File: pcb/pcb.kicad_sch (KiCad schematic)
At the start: 3 parts, among them U2 ESP32-C6-MINI-1

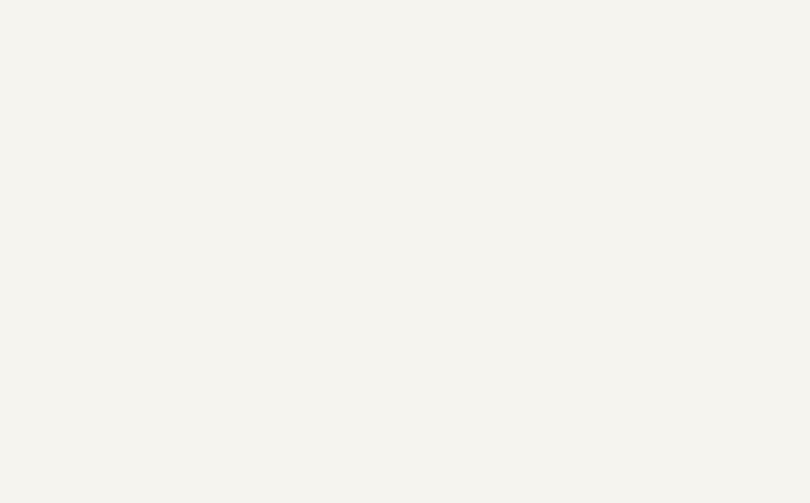
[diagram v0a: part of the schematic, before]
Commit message: adding the lightresistor with the voltage devider circuit
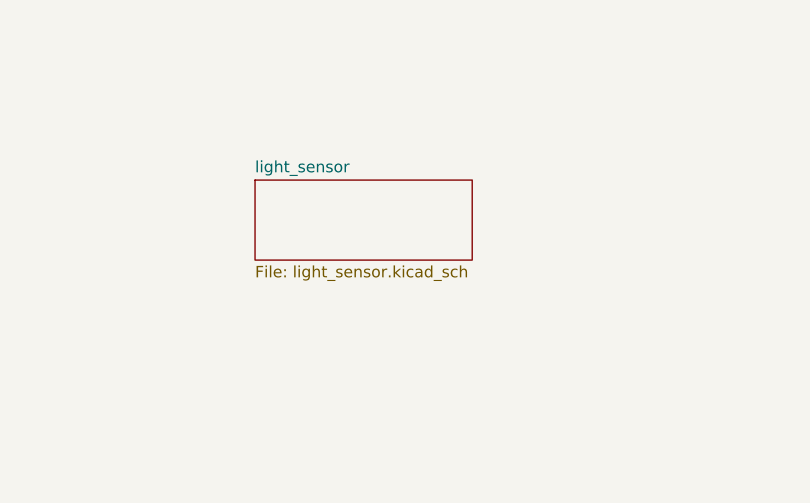
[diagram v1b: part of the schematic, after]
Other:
- added sheet light_sensor (light_sensor.kicad_sch)
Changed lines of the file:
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@@
+	)
+	(sheet
+		(at 91.44 34.29)
+		(size 24.13 8.89)
+		(exclude_from_sim no)
+		(in_bom yes)
+		(on_board yes)
+		(dnp no)
+		(fields_autoplaced yes)
+		(stroke
+			(width 0.1524)
+			(type solid)
+		)
+		(fill
+			(color 0 0 0 0.0000)
+		)
+		(property "Sheetname" "light_sensor"
+			(at 91.44 33.5784 0)
+			(effects
+				(font
+					(size 1.27 1.27)
+				)
+				(justify left bottom)
+			)
+		)
+		(property "Sheetfile" "light_sensor.kicad_sch"
+			(at 91.44 43.7646 0)
+			(effects
+				(font
+					(size 1.27 1.27)
+				)
+				(justify left top)
+			)
+		)
+		(instances
+			(project "pcb"
+				(path "/2955ee96-3683-4cf6-bfa3-83b5e4980920"
+					(page "8")
+				)
+			)
+		)
 	)
 	(sheet

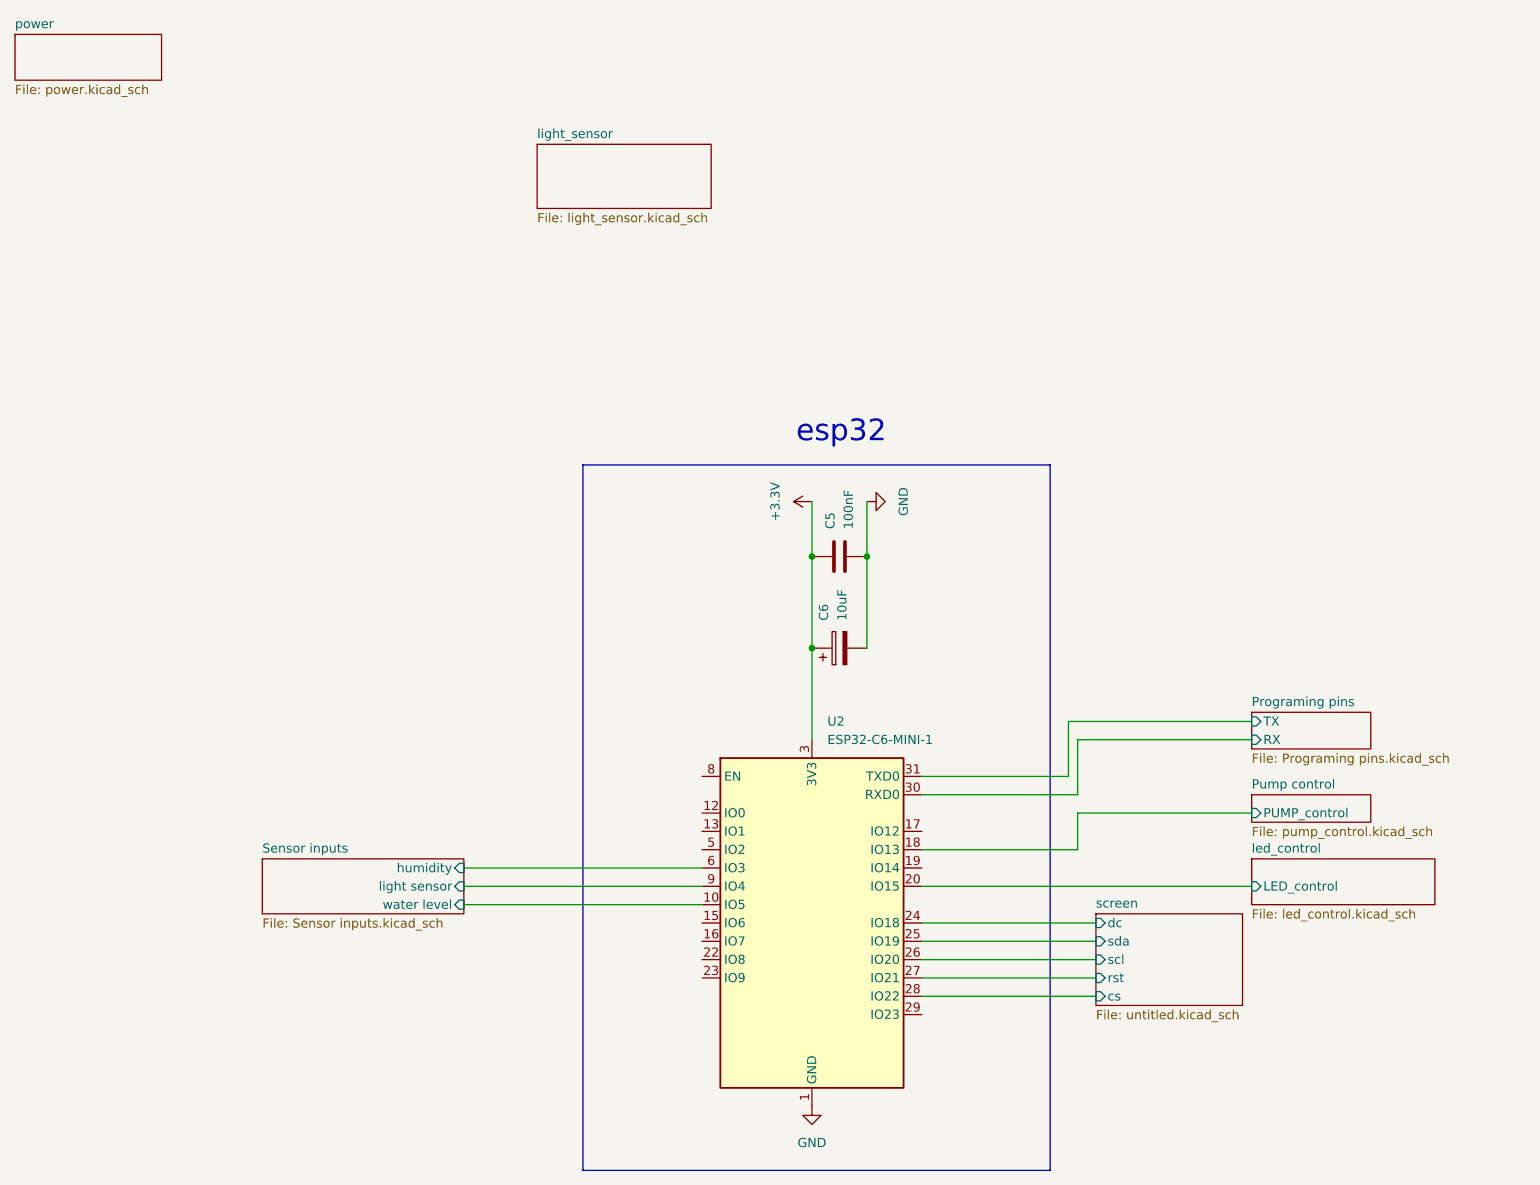
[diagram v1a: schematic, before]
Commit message: redesigning the circuit of the rellay and starting to adjust the footprints
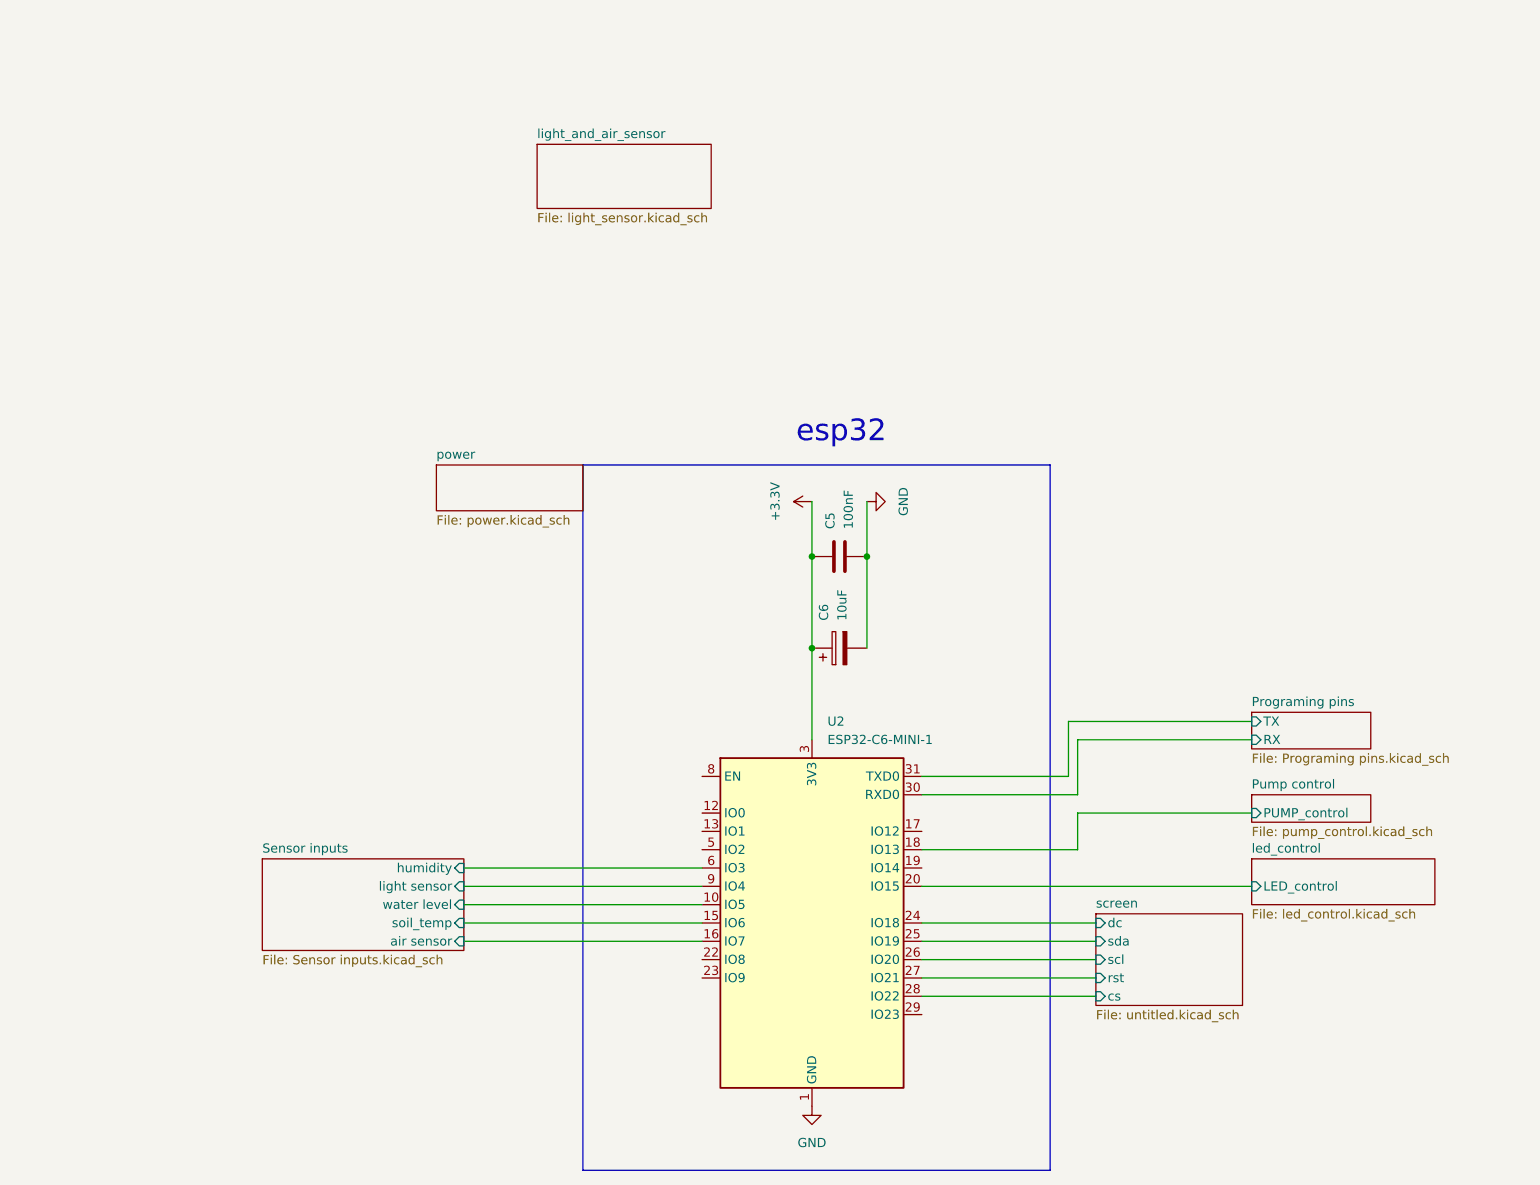
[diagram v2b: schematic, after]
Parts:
- C5: footprint (none) -> Resistor_SMD:R_0603_1608Metric_Pad0.98x0.95mm_HandSolder
- C6: footprint (none) -> Capacitor_THT:CP_Radial_D5.0mm_P2.50mm
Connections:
- net Sensor inputs/soil_temp: now reaches U2.15 (IO6)
- net Sensor inputs/air sensor: now reaches U2.16 (IO7)
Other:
- sheet light_sensor renamed light_and_air_sensor
- sheet Sensor inputs ports: added air sensor, soil_temp; removed none
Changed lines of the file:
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@@
+	(wire
+		(pts
+			(xy 81.28 142.24) (xy 114.3 142.24)
+		)
+		(stroke
+			(width 0)
+			(type default)
+		)
+	)
 	(wire
 		(pts
@@
 		(pts
 			(xy 81.28 137.16) (xy 114.3 137.16)
+		)
+		(stroke
+			(width 0)
+			(type default)
+		)
+	)
+	(wire
+		(pts
+			(xy 81.28 144.78) (xy 114.3 144.78)
 		)
 		(stroke
@@
 			)
 		)
-		(property "Footprint" ""
+		(property "Footprint" "Capacitor_THT:CP_Radial_D5.0mm_P2.50mm"
 			(at 137.16 103.1748 0)
 			(effects
@@
 		)
 		(property "Description" "Polarized capacitor"
+			(at 133.35 104.14 0)
+			(effects
+				(font
+					(size 1.27 1.27)
+				)
+				(hide yes)
+			)
+		)
+		(property "amazon link" ""
 			(at 133.35 104.14 0)
 			(effects
@@
 			)
 		)
-		(property "Footprint" ""
+		(property "Footprint" "Resistor_SMD:R_0603_1608Metric_Pad0.98x0.95mm_HandSolder"
 			(at 137.16 90.4748 0)
 			(effects
@@
 		)
 		(property "Description" "Unpolarized capacitor"
+			(at 133.35 91.44 0)
+			(effects
+				(font
+					(size 1.27 1.27)
+				)
+				(hide yes)
+			)
+		)
+		(property "amazon link" ""
 			(at 133.35 91.44 0)
 			(effects
@@
 			)
 		)
+		(property "amazon link" ""
+			(at 129.54 142.24 0)
+			(effects
+				(font
+					(size 1.27 1.27)
+				)
+				(hide yes)
+			)
+		)
 		(pin "40"
 		)
@@
 	)
 	(sheet
-		(at 19.05 19.05)
+		(at 77.47 78.74)
 		(size 20.32 6.35)
 		(exclude_from_sim no)
@@
 		)
 		(property "Sheetname" "power"
-			(at 19.05 18.3384 0)
+			(at 77.47 78.0284 0)
 			(effects
 				(font
@@
 		)
 		(property "Sheetfile" "power.kicad_sch"
-			(at 19.05 25.9846 0)
+			(at 77.47 85.6746 0)
 			(effects
 				(font
@@
 			(color 0 0 0 0.0000)
 		)
-		(property "Sheetname" "light_sensor"
+		(property "Sheetname" "light_and_air_sensor"
 			(at 91.44 33.5784 0)
 			(effects
@@
 	(sheet
 		(at 53.34 133.35)
-		(size 27.94 7.62)
+		(size 27.94 12.7)
 		(exclude_from_sim no)
 		(in_bom yes)
@@
 		)
 		(property "Sheetfile" "Sensor inputs.kicad_sch"
-			(at 53.34 141.5546 0)
+			(at 53.34 146.6346 0)
 			(effects
 				(font
@@
 			(effects
 				(font
+					(size 1.27 1.27)
+				)
+				(justify right)
+			)
+		)
+		(pin "soil_temp" input
+			(at 81.28 142.24 0)
+			(effects
+				(font
+					(size 1.27 1.27)
+				)
+				(justify right)
+			)
+		)
+		(pin "air sensor" input
+			(at 81.28 144.78 0)
+			(effects
+				(font

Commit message: finishing the bom and adding the jlc number of the parts
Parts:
- C5: jlc part # (none) -> C1591
- C6: jlc part # (none) -> C216288
- U2: jlc part # (none) -> C5736265
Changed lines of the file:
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@@
+			)
+		)
+		(property "jlc part #" "C216288"
+			(at 133.35 104.14 0)
+			(effects
+				(font
+					(size 1.27 1.27)
+				)
+				(hide yes)
 			)
 		)
@@
 			)
 		)
+		(property "jlc part #" "C1591"
+			(at 133.35 91.44 0)
+			(effects
+				(font
+					(size 1.27 1.27)
+				)
+				(hide yes)
+			)
+		)
 		(pin "2"
 		)
@@
 			)
 		)
+		(property "jlc part #" "C5736265"
+			(at 129.54 142.24 0)
+			(effects
+				(font
+					(size 1.27 1.27)
+				)
+				(hide yes)
+			)
+		)
 		(pin "40"
 		)
@@
 	)
 	(sheet
-		(at 91.44 34.29)
-		(size 24.13 8.89)
+		(at 162.56 78.74)
+		(size 20.32 6.35)
 		(exclude_from_sim no)
 		(in_bom yes)
@@
 		)
 		(property "Sheetname" "light_and_air_sensor"
-			(at 91.44 33.5784 0)
+			(at 162.56 78.0284 0)
 			(effects
 				(font
@@
 		)
 		(property "Sheetfile" "light_sensor.kicad_sch"
-			(at 91.44 43.7646 0)
-			(effects
-				(font
+			(at 162.56 85.6746 0)
+			(effects
+				(font

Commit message: realigning the pcb
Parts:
- U2: footprint RF_Module:ESP32-C6-MINI-1 -> Library:ESP32-C6-MINI-1psa
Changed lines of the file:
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@@
 			)
 		)
-		(property "Footprint" "RF_Module:ESP32-C6-MINI-1"
+		(property "Footprint" "Library:ESP32-C6-MINI-1psa"
 			(at 147.32 167.64 0)
 			(effects
